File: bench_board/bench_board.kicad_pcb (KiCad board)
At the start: 4 copper layers, 80 x 60 mm, 65 parts, among them J1 BATT_4S, J10 BUZZER, J2 BOOT0_JUMPER, J3 USB-C, J4 CRSF_UART, J5 DSHOT_M1-M4, J6 SWD, J7 RX_PWR_5V, J8 TELEM_TX, J9 EXPANSION_BUS, Q1 AO3400A, U1 STM32F405RGT6, U2 TPS54336ADDA, U4 MPU-6000, U5 USBLC6-2SC6, U6 MT3608, Y1 8MHz

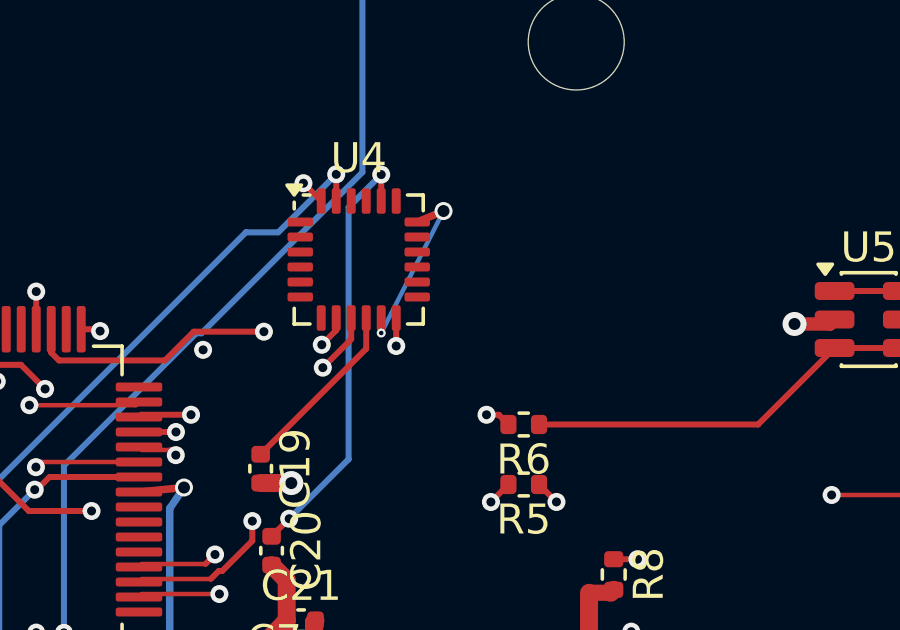
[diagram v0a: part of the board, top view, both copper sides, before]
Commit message: Board: U4.13 closed -- stub + tip via + B.Cu leg + landing via. 10 -> 9 (guard 53/9/93)
Attempt 2, with the refill in the loop. Attempt 1 connected (10 -> 9)
but collided with the stored In1 GND fill at both new via positions --
the exact class of error the guard exists to catch, and it did.

Co-Authored-By: Claude Opus 5 <noreply@anthropic.com>
Claude-Session: https://claude.ai/code/session_013j3hUNiKQb8Wi66Tf5nVkP
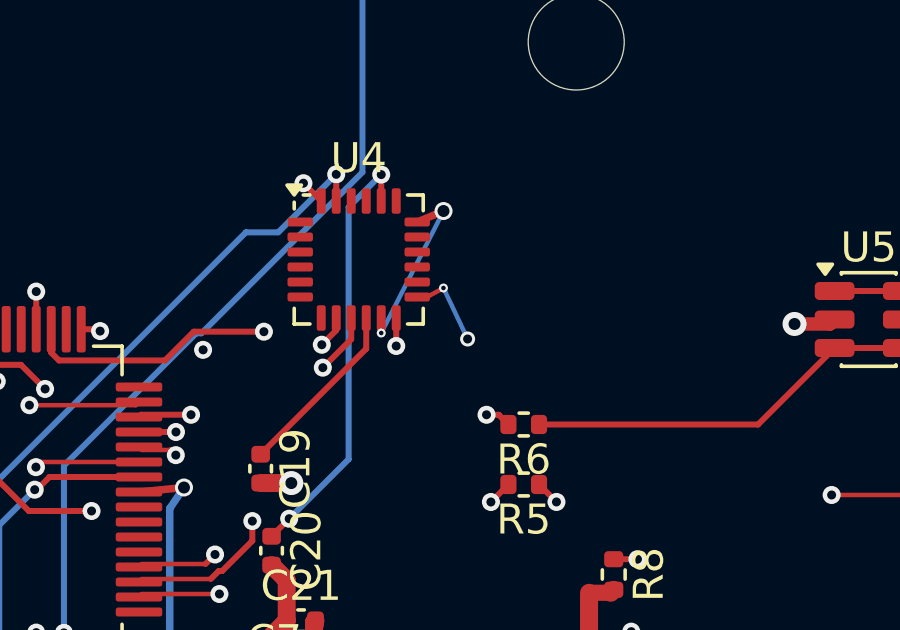
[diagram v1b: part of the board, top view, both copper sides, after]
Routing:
- net /3V3: track 45.7 -> 48.2 mm, vias 6 -> 8
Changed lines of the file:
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@@
+	)
+	(segment
+		(start 50.28 23.25)
+		(end 50.825 22.95)
+		(width 0.15)
+		(layer "F.Cu")
+		(net "/3V3")
 	)
 	(segment
@@
 	)
 	(via
+		(at 50.825 22.95)
+		(size 0.3)
+		(drill 0.15)
+		(layers "F.Cu" "B.Cu")
+		(net "/3V3")
+	)
+	(via
+		(at 51.63 24.65)
+		(size 0.5)
+		(drill 0.3)
+		(layers "F.Cu" "B.Cu")
+		(net "/3V3")
+	)
+	(via
 		(at 44.3702 42.2805)
 		(size 0.6)
@@
 		(net "/3V3")
 	)
+	(segment
+		(start 50.825 22.95)
+		(end 51.63 24.65)
+		(width 0.15)
+		(layer "B.Cu")
+		(net "/3V3")
+	)

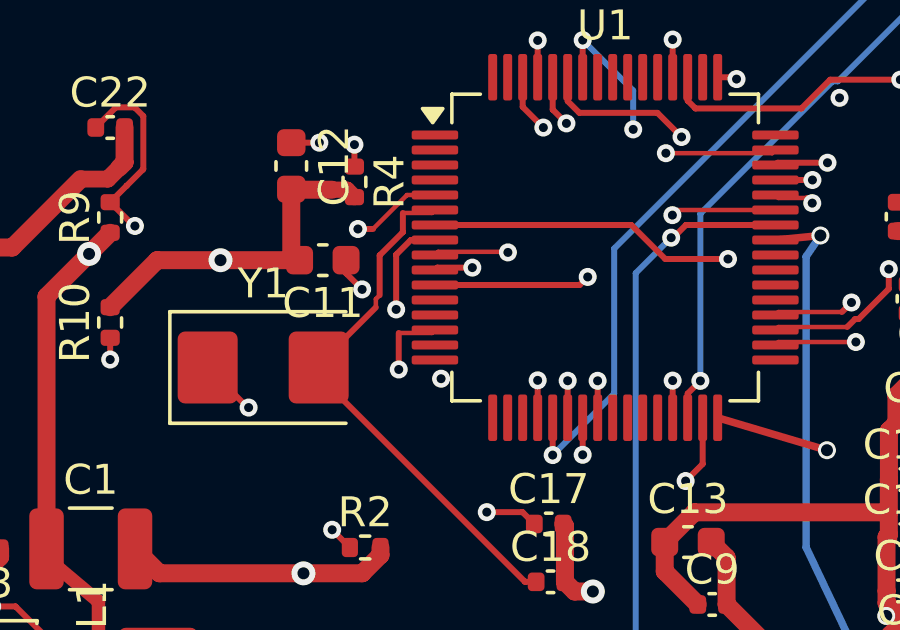
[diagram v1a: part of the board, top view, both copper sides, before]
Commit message: Board: U1.13 closed -- in-pad 0.30/0.15 via + B.Cu to a landing under the chip body. 9 -> 8
First of the in-pad set: the via drill sits inside the 0.30 mm-wide LQFP
pad, so this pad joins the epoxy-fill-and-cap list for the order sheet.
The exact-0.200 clearance to the neighbouring pad passed DRC as computed.
Guard 53/8/93, ratcheted.

Co-Authored-By: Claude Opus 5 <noreply@anthropic.com>
Claude-Session: https://claude.ai/code/session_013j3hUNiKQb8Wi66Tf5nVkP
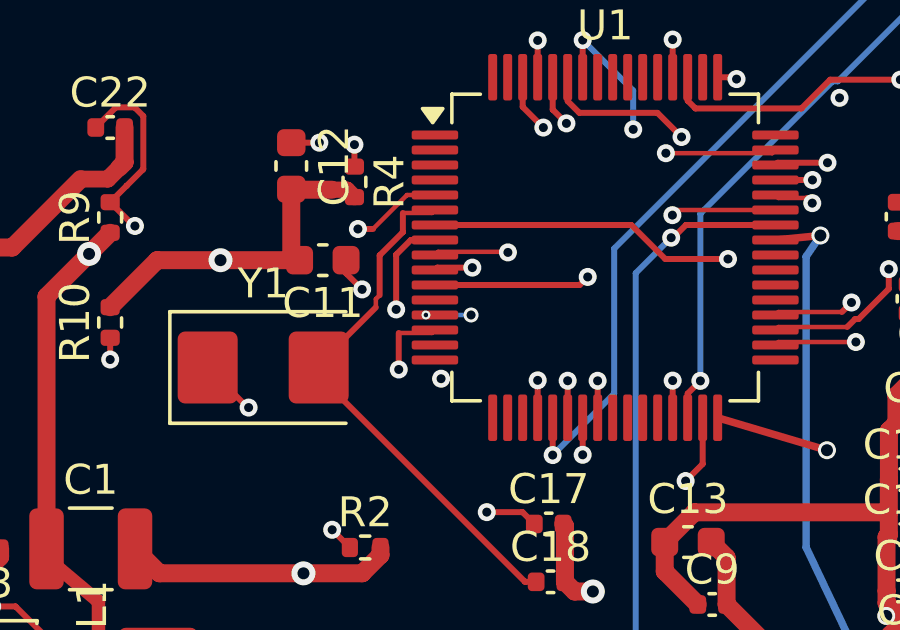
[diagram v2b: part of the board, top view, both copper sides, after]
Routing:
- net /3V3: track 48.2 -> 49.7 mm, vias 8 -> 10
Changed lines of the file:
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@@
+	)
+	(via
+		(at 30.53 32.25)
+		(size 0.5)
+		(drill 0.3)
+		(layers "F.Cu" "B.Cu")
+		(net "/3V3")
 	)
 	(via
@@
 	)
 	(via
+		(at 29.025 32.25)
+		(size 0.3)
+		(drill 0.15)
+		(layers "F.Cu" "B.Cu")
+		(net "/3V3")
+	)
+	(via
 		(at 17.2058 9.1762)
 		(size 0.8)
@@
 		(net "/3V3")
 	)
+	(segment
+		(start 29.025 32.25)
+		(end 30.53 32.25)
+		(width 0.15)
+		(layer "B.Cu")
+		(net "/3V3")
+	)

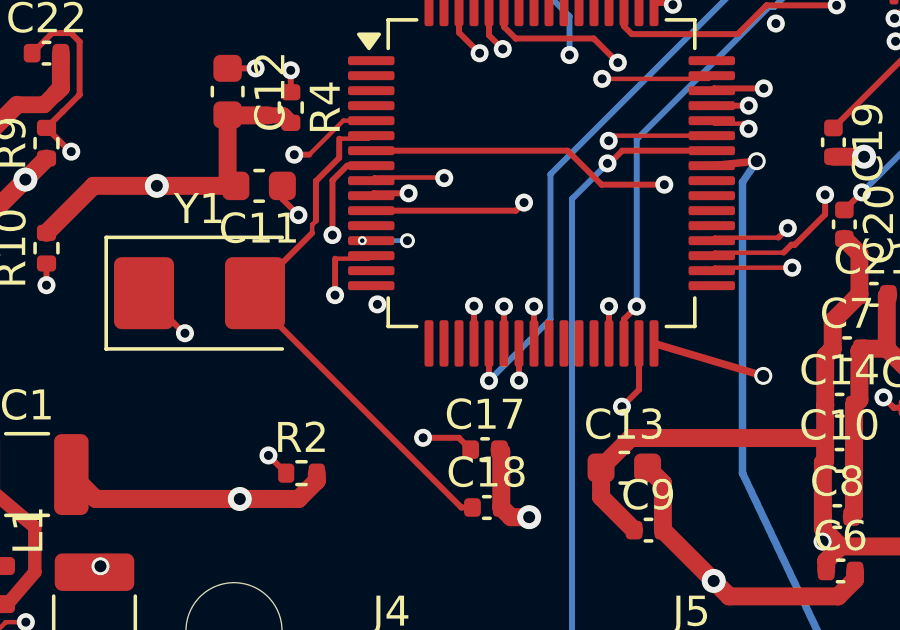
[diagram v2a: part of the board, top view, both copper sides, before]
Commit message: Board: U1.19 closed -- in-pad via + B.Cu leg. 8 -> 7 (guard 53/7/93)
Co-Authored-By: Claude Opus 5 <noreply@anthropic.com>
Claude-Session: https://claude.ai/code/session_013j3hUNiKQb8Wi66Tf5nVkP
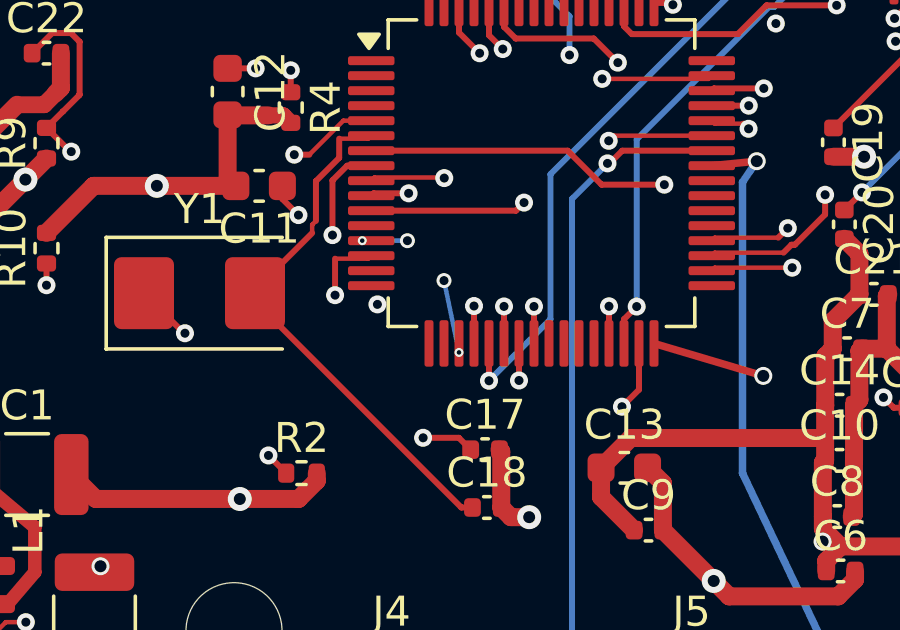
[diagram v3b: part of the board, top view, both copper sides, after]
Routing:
- net /3V3: track 49.7 -> 52.1 mm, vias 10 -> 12
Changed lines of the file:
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@@
+	)
+	(via
+		(at 31.75 33.58)
+		(size 0.5)
+		(drill 0.3)
+		(layers "F.Cu" "B.Cu")
+		(net "/3V3")
 	)
 	(via
@@
 		(size 0.6)
 		(drill 0.4)
+		(layers "F.Cu" "B.Cu")
+		(net "/3V3")
+	)
+	(via
+		(at 32.25 35.975)
+		(size 0.3)
+		(drill 0.15)
 		(layers "F.Cu" "B.Cu")
 		(net "/3V3")
@@
 		(width 0.15)
 		(layer "B.Cu")
+		(net "/3V3")
+	)
+	(segment
+		(start 32.25 35.975)
+		(end 31.75 33.58)
+		(width 0.15)
+		(layer "B.Cu")

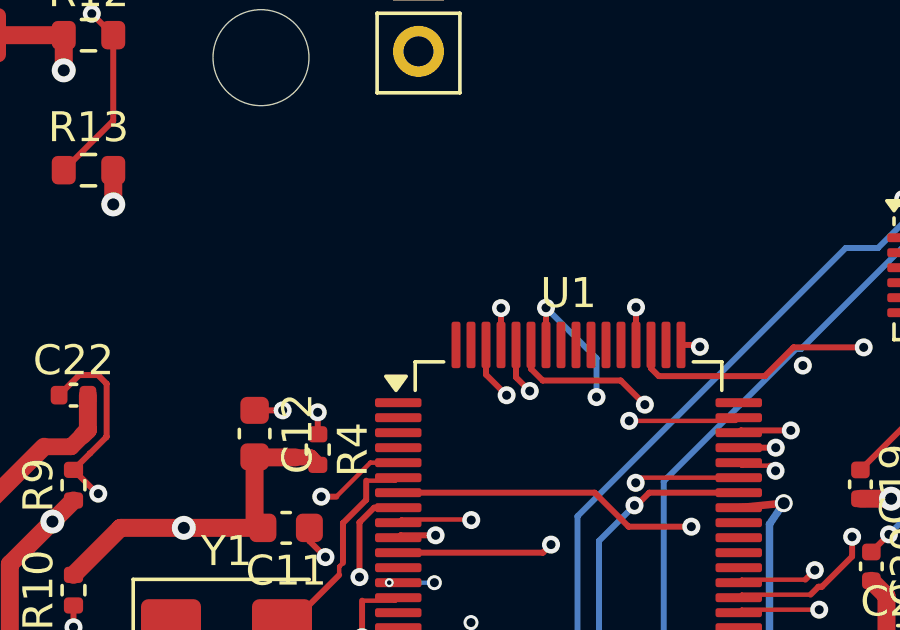
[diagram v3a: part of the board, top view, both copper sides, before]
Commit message: Board: U1.63 closed -- in-pad via + B.Cu leg. 7 -> 6 (guard 53/6/93)
Co-Authored-By: Claude Opus 5 <noreply@anthropic.com>
Claude-Session: https://claude.ai/code/session_013j3hUNiKQb8Wi66Tf5nVkP
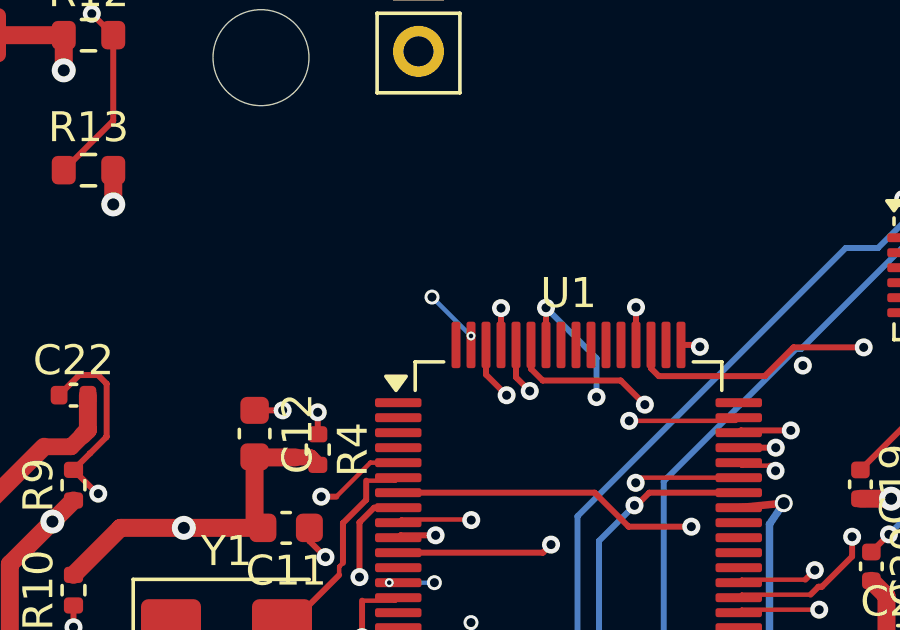
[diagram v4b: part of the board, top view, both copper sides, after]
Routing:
- net /GND: track 119.4 -> 121.2 mm, vias 15 -> 17
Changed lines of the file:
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@@
+	)
+	(via
+		(at 30.45 22.73)
+		(size 0.5)
+		(drill 0.3)
+		(layers "F.Cu" "B.Cu")
+		(net "/GND")
 	)
 	(via
@@
 	)
 	(via
+		(at 31.75 24.025)
+		(size 0.3)
+		(drill 0.15)
+		(layers "F.Cu" "B.Cu")
+		(net "/GND")
+	)
+	(via
 		(at 15.5546 47.9869)
 		(size 0.8)
@@
 		(width 0.15)
 		(layer "B.Cu")
+		(net "/GND")
+	)
+	(segment
+		(start 31.75 24.025)
+		(end 30.45 22.73)
+		(width 0.15)
+		(layer "B.Cu")

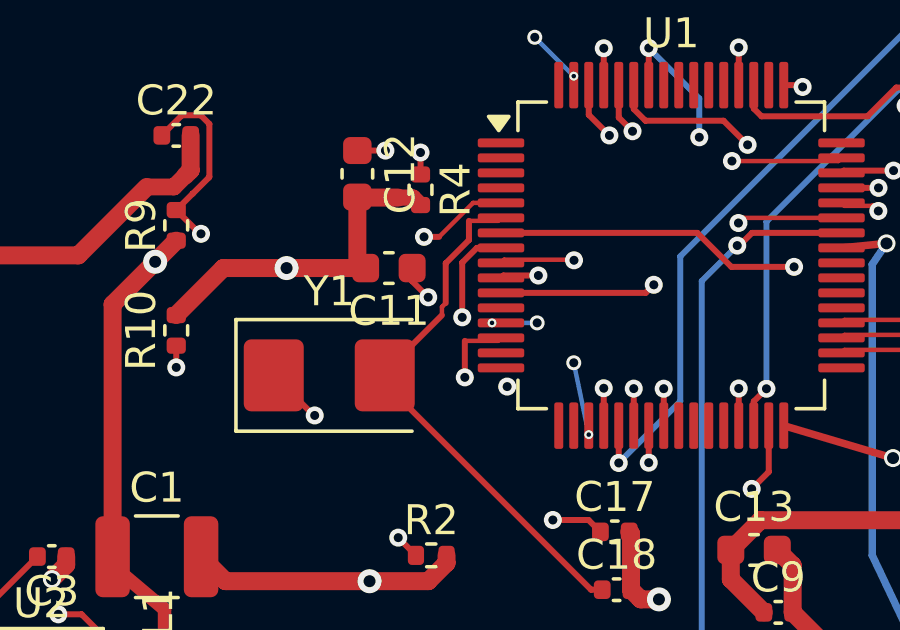
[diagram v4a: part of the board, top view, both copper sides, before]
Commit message: Board: U1.12 closed on attempt 2 -- western B.Cu detour. 6 -> 5 (guard 53/5/93)
Attempt 1's direct leg was blocked by MY OWN U1.13 route -- the two
squeeze the same inter-pad corridor, and the guard caught the collision
between the new GND leg and the day-old 3V3 leg (0.324 mm where 0.425 is
needed). The detour runs south, west past the CS1/VCAP1/HSE_IN via
minefield with verified berths (min 0.61 mm centre distance), north
outside it, then into the same landing. 9.3 mm of B.Cu for one pin, and
worth it.

Co-Authored-By: Claude Opus 5 <noreply@anthropic.com>
Claude-Session: https://claude.ai/code/session_013j3hUNiKQb8Wi66Tf5nVkP
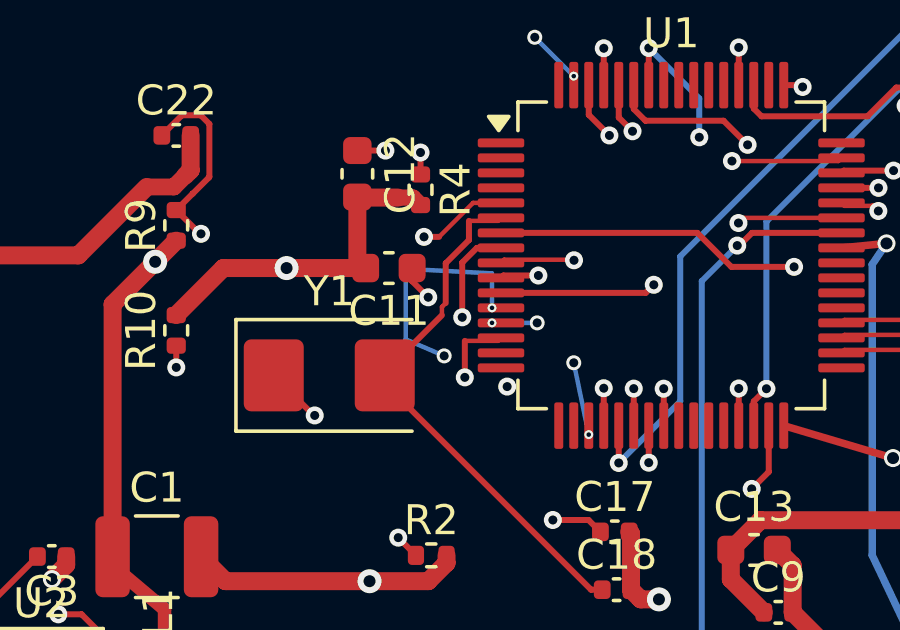
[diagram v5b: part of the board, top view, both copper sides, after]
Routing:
- net /GND: track 121.2 -> 129.0 mm, vias 17 -> 19
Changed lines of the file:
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@@
+	)
+	(via
+		(at 27.43 33.35)
+		(size 0.5)
+		(drill 0.3)
+		(layers "F.Cu" "B.Cu")
+		(net "/GND")
 	)
 	(via
@@
 	)
 	(via
+		(at 29.025 31.75)
+		(size 0.3)
+		(drill 0.15)
+		(layers "F.Cu" "B.Cu")
+		(net "/GND")
+	)
+	(via
 		(at 45.7528 29.452)
 		(size 0.8)
@@
 		(net "/GND")
 	)
+	(segment
+		(start 29.025 31.75)
+		(end 29.025 30.6)
+		(width 0.15)
+		(layer "B.Cu")
+		(net "/GND")
+	)
+	(segment
+		(start 26.15 30.45)
+		(end 26.15 32.8)
+		(width 0.15)
+		(layer "B.Cu")
+		(net "/GND")
+	)
+	(segment
+		(start 29.025 30.6)
+		(end 26.15 30.45)
+		(width 0.15)
+		(layer "B.Cu")
+		(net "/GND")
+	)
+	(segment
+		(start 26.15 32.8)
+		(end 27.43 33.35)
+		(width 0.15)
+		(layer "B.Cu")
+		(net "/GND")
+	)

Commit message: Board: U1.1 closed -- 0.65 mm F.Cu stub through the /EXP_SPI_CS1 shadow, tip via, B.Cu leg. 5 -> 4 (guard 53/4/93)
CS1 runs the whole left column on In1.Cu 0.665 mm from the pad centres,
which is what killed every tip and in-pad site here: a through-via body
cannot clear it. The site at lon 1.425 is past CS1's shadow; the stub
that reaches it lives on F.Cu and legitimately flies OVER CS1 -- the
checker itself had to be taught that (it was testing F.Cu stubs against
inner-layer segments and rejecting every site on the column).

Co-Authored-By: Claude Opus 5 <noreply@anthropic.com>
Claude-Session: https://claude.ai/code/session_013j3hUNiKQb8Wi66Tf5nVkP
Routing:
- net /3V3: track 52.1 -> 55.7 mm, vias 12 -> 14
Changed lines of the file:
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@@
+	)
+	(segment
+		(start 28.55 26.25)
+		(end 27.9 26.375)
+		(width 0.15)
+		(layer "F.Cu")
+		(net "/3V3")
 	)
 	(segment
@@
 	)
 	(via
+		(at 25.8 24.28)
+		(size 0.5)
+		(drill 0.3)
+		(layers "F.Cu" "B.Cu")
+		(net "/3V3")
+	)
+	(via
 		(at 31.75 33.58)
 		(size 0.5)
@@
 	)
 	(via
+		(at 27.9 26.375)
+		(size 0.3)
+		(drill 0.15)
+		(layers "F.Cu" "B.Cu")
+		(net "/3V3")
+	)
+	(via
 		(at 17.2058 9.1762)
 		(size 0.8)
@@
 		(width 0.15)
 		(layer "B.Cu")
+		(net "/3V3")
+	)
+	(segment
+		(start 27.9 26.375)
+		(end 25.8 24.28)
+		(width 0.15)
+		(layer "B.Cu")

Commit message: Board: U1.18 closed -- deep in-pad via (lon 0.15) + B.Cu dodge around VBAT_SENSE. 4 -> 3 (guard 53/3/93)
The site search's floor was lon 0.30, where /VCAP1 on In2 blocks by
48 um; the blocker FADES INWARD and lon 0.10-0.25 is legal. The search
tool encoded an assumption the geometry did not share.

Co-Authored-By: Claude Opus 5 <noreply@anthropic.com>
Claude-Session: https://claude.ai/code/session_013j3hUNiKQb8Wi66Tf5nVkP
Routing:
- net /GND: track 129.0 -> 134.8 mm, vias 19 -> 20
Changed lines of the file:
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@@
+		(net "/GND")
+	)
+	(via
+		(at 31.75 35.825)
+		(size 0.3)
+		(drill 0.15)
+		(layers "F.Cu" "B.Cu")
 		(net "/GND")
 	)
@@
 	)
 	(segment
+		(start 28.3 35.2)
+		(end 27.2 34.2)
+		(width 0.15)
+		(layer "B.Cu")
+		(net "/GND")
+	)
+	(segment
 		(start 26.15 32.8)
 		(end 27.43 33.35)
@@
 		(width 0.15)
 		(layer "B.Cu")
+		(net "/GND")
+	)
+	(segment
+		(start 31.75 35.825)
+		(end 28.3 35.2)
+		(width 0.15)
+		(layer "B.Cu")
+		(net "/GND")
+	)
+	(segment
+		(start 27.2 34.2)
+		(end 27.43 33.35)
+		(width 0.15)
+		(layer "B.Cu")

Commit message: Board: U1.64 closed -- 1.6 mm interior diagonal to the now-connected pad 1. 3 -> 2 (guard 53/2/93)
U1 has no interior keepout (U4 does -- its 'empty' interior turned out to
be enforced by a rule area, which is what killed U4.1's third strike).
Pad 64's own tip band is blocked on three layers at once (my new U1.63
GND leg on B.Cu, /EXP_SPI_CS1 and /CRSF_RX on In1), but its corner
neighbour pad 1 is 3V3 and now plane-connected, and the LQFP interior
between their inner tips is genuinely empty.

THE SCORE: 11 of 13 closed. The two remaining are each proven
unclosable in scope three independent ways:

  U1.48 [3V3/VDD_3]: the /EXP_I2C_SDA B.Cu diagonal passes essentially
  through the pad position (7 um off) so no in-pad or tip via can exist
  on B.Cu; In1 (/EXP_SPI_SCK -0.217) and In2 (/SPI1_CS -0.226) block the
  barrel at every probed offset; and the LQFP interior south is walled by
  VCAP2 + TELEM_TX + the NRST/CRSF system spanning x 29.3-40.7.

  U4.1 [GND/CLKIN-tie]: fenced north by the MOSI/SCK/CPOUT via row plus
  the SDA vertical, east by the paired SCK/SDA diagonals and the CPOUT
  vertical, south by the CS/MISO/REGOUT via stack, west by 4 mm of
  fill-free carve -- and the interior is a tracks-forbidden rule area
  (items_not_allowed, found on the third strike).

Both are bench-tolerable and go on the order sheet with their function
and consequence stated plainly.

Co-Authored-By: Claude Opus 5 <noreply@anthropic.com>
Claude-Session: https://claude.ai/code/session_013j3hUNiKQb8Wi66Tf5nVkP
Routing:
- net /3V3: track 55.7 -> 57.4 mm
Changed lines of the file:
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@@
+	)
+	(segment
+		(start 31.25 25.1)
+		(end 30.1 26.25)
+		(width 0.15)
+		(layer "F.Cu")
+		(net "/3V3")
 	)
 	(segment
